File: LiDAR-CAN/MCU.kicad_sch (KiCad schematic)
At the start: 25 parts, among them J2 61300511121, SW1 RST, U1 STM32F401RBTx, Y3 25MHz

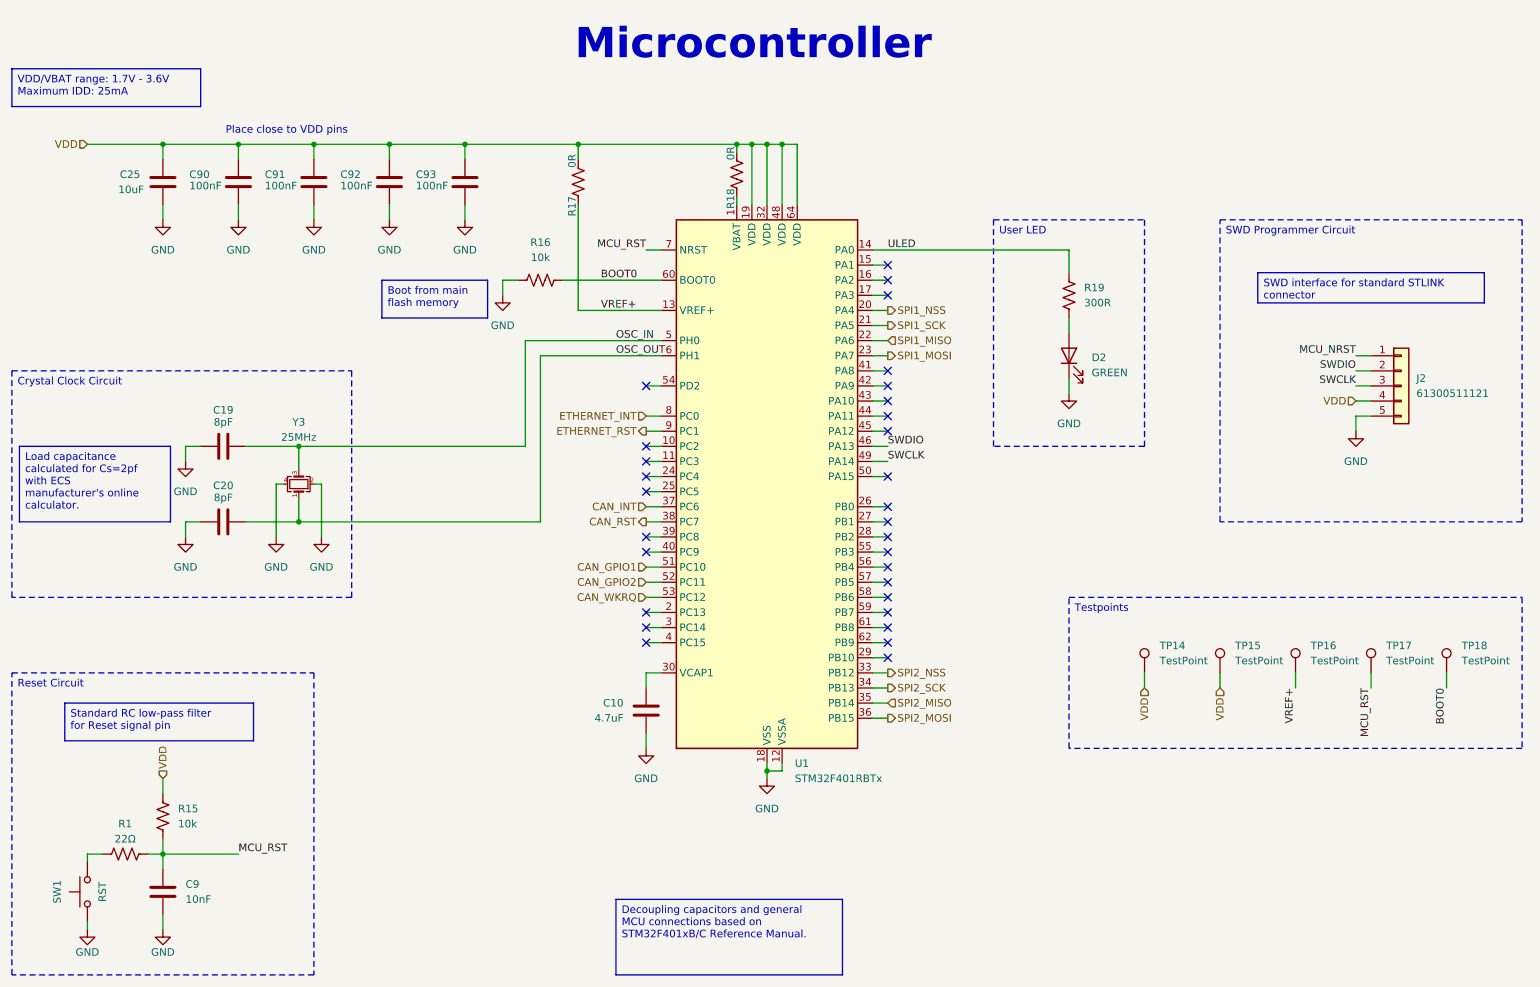
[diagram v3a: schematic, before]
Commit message: Add power management circuit
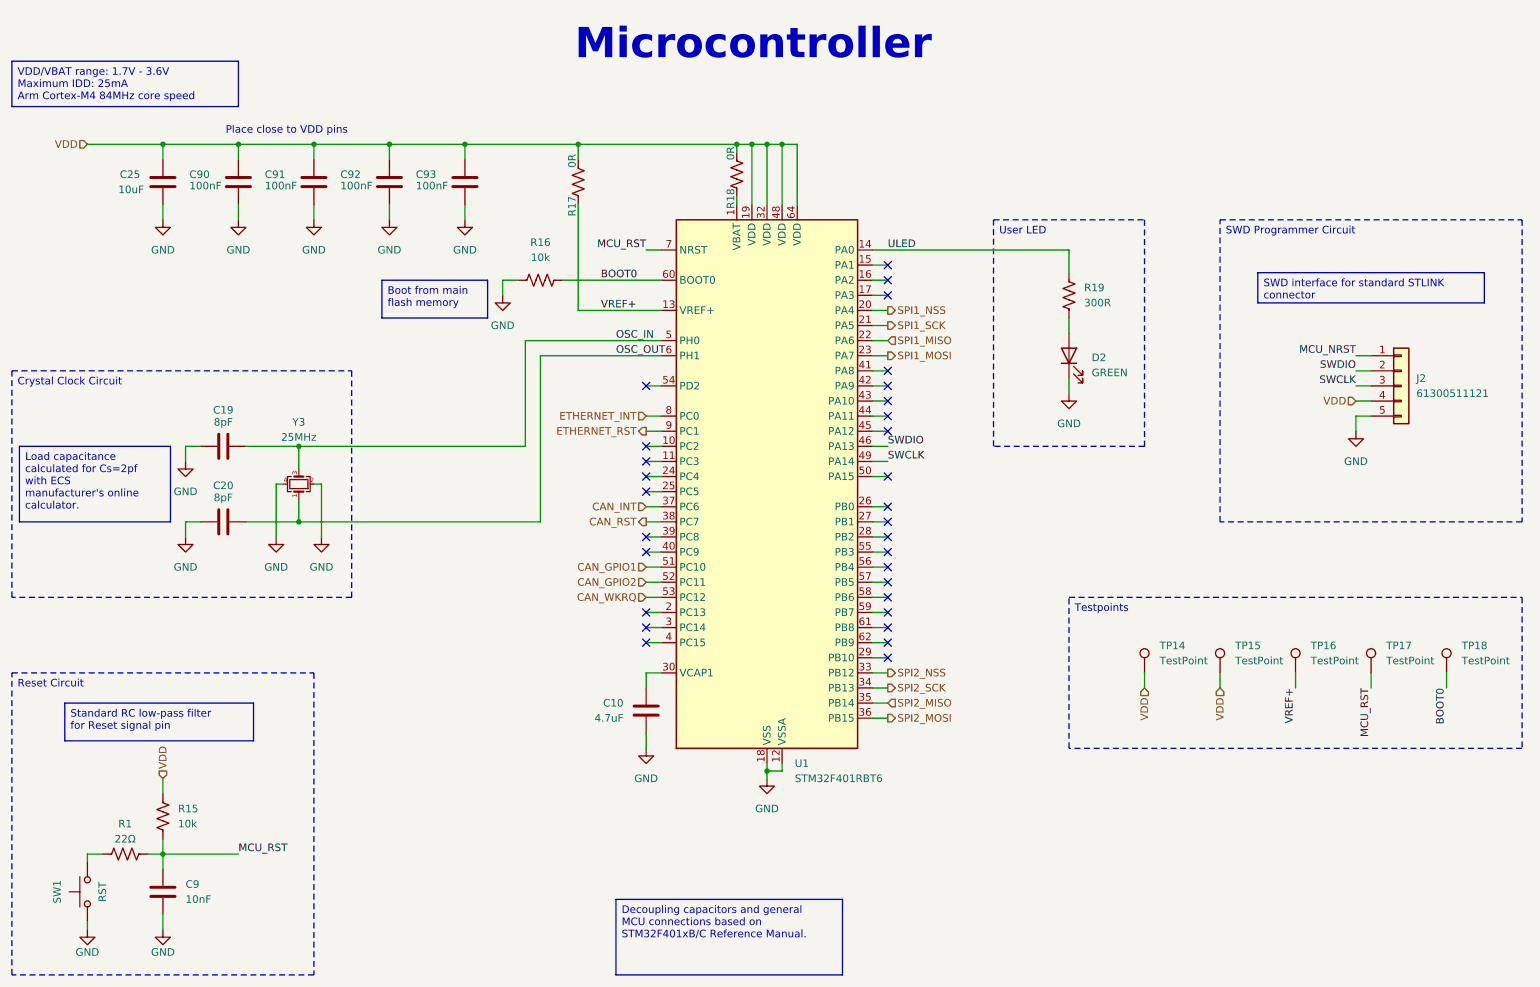
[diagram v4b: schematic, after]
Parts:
- U1: value STM32F401RBTx -> STM32F401RBT6; MPN (none) -> STM32F401RBT6; Manufacturer (none) -> STMicroelectronics
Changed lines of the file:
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@@
 		)
 	)
-	(text_box "VDD/VBAT range: 1.7V - 3.6V\nMaximum IDD: 25mA"
+	(text_box "VDD/VBAT range: 1.7V - 3.6V\nMaximum IDD: 25mA\nArm Cortex-M4 84MHz core speed"
 		(exclude_from_sim no)
-		(at 25.4 25.4 0)
-		(size 31.75 6.35)
+		(at 25.4 24.13 0)
+		(size 38.1 7.62)
 		(margins 0.9525 0.9525 0.9525 0.9525)
 		(stroke
@@
 			)
 		)
-		(property "Description" "0.1 µF ±10% 50V Ceramic Capacitor X7R 0603 (1608 Metric)"
+		(property "Description" "CAP CER 0.1UF 50V X7R 0603"
 			(at 101.6 44.45 0)
 			(effects
@@
 			)
 		)
-		(property "Description" "0.1 µF ±10% 50V Ceramic Capacitor X7R 0603 (1608 Metric)"
+		(property "Description" "CAP CER 0.1UF 50V X7R 0603"
 			(at 76.2 44.45 0)
 			(effects
@@
 			)
 		)
-		(property "Description" "0.1 µF ±10% 50V Ceramic Capacitor X7R 0603 (1608 Metric)"
+		(property "Description" "CAP CER 0.1UF 50V X7R 0603"
 			(at 88.9 44.45 0)
 			(effects
@@
 			)
 		)
-		(property "Value" "STM32F401RBTx"
+		(property "Value" "STM32F401RBT6"
 			(at 157.0833 144.78 0)
 			(effects
@@
 			)
 		)
-		(property "Description" "STMicroelectronics Arm Cortex-M4 MCU, 128KB flash, 64KB RAM, 84 MHz, 1.7-3.6V, 50 GPIO, LQFP64"
+		(property "Description" "IC MCU 32BIT 128KB FLASH 64LQFP"
+			(at 152.4 96.52 0)
+			(effects
+				(font
+					(size 1.27 1.27)
+				)
+				(hide yes)
+			)
+		)
+		(property "Manufacturer" "STMicroelectronics"
+			(at 152.4 96.52 0)
+			(effects
+				(font
+					(size 1.27 1.27)
+				)
+				(hide yes)
+			)
+		)
+		(property "MPN" "STM32F401RBT6"
 			(at 152.4 96.52 0)
 			(effects
@@
 			)
 		)
-		(property "Description" "0.1 µF ±10% 50V Ceramic Capacitor X7R 0603 (1608 Metric)"
+		(property "Description" "CAP CER 0.1UF 50V X7R 0603"
 			(at 63.5 44.45 0)
 			(effects

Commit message: Add power management connections in Root sheet
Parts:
- R17, R18: footprint Resistor_SMD:R_0805_2012Metric -> Resistor_SMD:R_0603_1608Metric; MPN ERJ-6GEY0R00V -> RC0603JR-070RL; Manufacturer (none) -> YAGEO; SPN P0.0ACT-ND -> (none)
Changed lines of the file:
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@@
 			)
 		)
-		(property "Footprint" "Resistor_SMD:R_0805_2012Metric"
+		(property "Footprint" "Resistor_SMD:R_0603_1608Metric"
 			(at 119.634 44.196 90)
 			(effects
@@
 			)
 		)
-		(property "Datasheet" "https://industrial.panasonic.com/ww/products/pt/general-purpose-chip-resistors/models/ERJ6GEY0R00V"
+		(property "Datasheet" "https://www.yageo.com/upload/media/product/products/datasheet/rchip/PYu-RC_Group_51_RoHS_L_12.pdf"
 			(at 120.65 44.45 0)
 			(effects
@@
 			)
 		)
-		(property "Description" "RES SMD 0 OHM JUMPER 1/8W 0805"
+		(property "Description" "RES 0 OHM JUMPER 1/10W 0603"
 			(at 120.65 44.45 0)
 			(effects
@@
 			)
 		)
-		(property "SPN" "P0.0ACT-ND"
+		(property "Manufacturer" "YAGEO"
 			(at 120.65 44.45 0)
 			(effects
@@
 			)
 		)
-		(property "MPN" "ERJ-6GEY0R00V"
+		(property "MPN" "RC0603JR-070RL"
 			(at 120.65 44.45 0)
 			(effects
@@
 			)
 		)
-		(property "Footprint" "Resistor_SMD:R_0805_2012Metric"
+		(property "Footprint" "Resistor_SMD:R_0603_1608Metric"
 			(at 146.304 42.926 90)
 			(effects
@@
 			)
 		)
-		(property "Datasheet" "https://industrial.panasonic.com/ww/products/pt/general-purpose-chip-resistors/models/ERJ6GEY0R00V"
+		(property "Datasheet" "https://www.yageo.com/upload/media/product/products/datasheet/rchip/PYu-RC_Group_51_RoHS_L_12.pdf"
 			(at 147.32 43.18 0)
 			(effects
@@
 			)
 		)
-		(property "Description" "RES SMD 0 OHM JUMPER 1/8W 0805"
+		(property "Description" "RES 0 OHM JUMPER 1/10W 0603"
 			(at 147.32 43.18 0)
 			(effects
@@
 			)
 		)
-		(property "SPN" "P0.0ACT-ND"
+		(property "Manufacturer" "YAGEO"
 			(at 147.32 43.18 0)
 			(effects
@@
 			)
 		)
-		(property "MPN" "ERJ-6GEY0R00V"
+		(property "MPN" "RC0603JR-070RL"
 			(at 147.32 43.18 0)
 			(effects

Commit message: Feature schematic revision 1
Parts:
- renumbered C25 to C34, C90 to C35, C91 to C36, C92 to C37, C93 to C38, C19 to C39, C20 to C40, C10 to C41, C9 to C42, D2 to D5, J2 to J5, R18 to R29, R17 to R30, R16 to R31, R19 to R32, R15 to R33, R1 to R34, TP14 to TP30, TP15 to TP31, TP16 to TP32, TP17 to TP33, TP18 to TP34, U1 to U5
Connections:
- net MCU_NRST is gone; now on net MCU_RST: J5.1 (Pin_1)

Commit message: Start placement of components
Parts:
- TP30, TP31, TP32, TP33, TP34: footprint TestPoint:TestPoint_Pad_D1.5mm -> TestPoint:TestPoint_Pad_D1.0mm
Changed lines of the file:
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@@
 		(exclude_from_sim no)
 		(in_bom no)
-		(on_board no)
+		(on_board yes)
 		(dnp no)
 		(fields_autoplaced yes)
@@
 			)
 		)
-		(property "Footprint" "TestPoint:TestPoint_Pad_D1.5mm"
+		(property "Footprint" "TestPoint:TestPoint_Pad_D1.0mm"
 			(at 233.68 127 0)
 			(effects
@@
 		(exclude_from_sim no)
 		(in_bom no)
-		(on_board no)
+		(on_board yes)
 		(dnp no)
 		(fields_autoplaced yes)
@@
 			)
 		)
-		(property "Footprint" "TestPoint:TestPoint_Pad_D1.5mm"
+		(property "Footprint" "TestPoint:TestPoint_Pad_D1.0mm"
 			(at 271.78 127 0)
 			(effects
@@
 		(exclude_from_sim no)
 		(in_bom no)
-		(on_board no)
+		(on_board yes)
 		(dnp no)
 		(fields_autoplaced yes)
@@
 			)
 		)
-		(property "Footprint" "TestPoint:TestPoint_Pad_D1.5mm"
+		(property "Footprint" "TestPoint:TestPoint_Pad_D1.0mm"
 			(at 246.38 127 0)
 			(effects
@@
 		(exclude_from_sim no)
 		(in_bom no)
-		(on_board no)
+		(on_board yes)
 		(dnp no)
 		(fields_autoplaced yes)
@@
 			)
 		)
-		(property "Footprint" "TestPoint:TestPoint_Pad_D1.5mm"
+		(property "Footprint" "TestPoint:TestPoint_Pad_D1.0mm"
 			(at 259.08 127 0)
 			(effects
@@
 		(exclude_from_sim no)
 		(in_bom no)
-		(on_board no)
+		(on_board yes)
 		(dnp no)
 		(fields_autoplaced yes)
@@
 			)
 		)
-		(property "Footprint" "TestPoint:TestPoint_Pad_D1.5mm"
+		(property "Footprint" "TestPoint:TestPoint_Pad_D1.0mm"
 			(at 220.98 127 0)
 			(effects
